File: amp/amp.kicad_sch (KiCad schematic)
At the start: 0 parts

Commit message: Initial circuit design (#2)
- Adds project description in README.md
- Populates schematic with initial circuit design
- Includes headphone output
- Adds future design to-dos
- Credits other designs influencing this project
- Extends ERC pre-commit triggers to any kicad file.
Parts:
- added C1, C5: 10nF, symbol Device:C
- added C2, C4: 2.2uF, symbol Device:C_Polarized
- added C3: 1nF, symbol Device:C
- added C6, C9: 100nF, symbol Device:C
- added C7: 220uF, symbol Device:C_Polarized
- added C8: 47nF, symbol Device:C
- added J1: Input, symbol Connector_Audio:AudioJack2
- added J2: Speaker 8Ω, symbol Connector_Audio:AudioJack2
- added J3: Headphones, symbol Connector_Audio:AudioJack2_SwitchT
- added R1, R2, R3, R4, R6, R9: 1M, symbol Device:R
- added R10, R7: 100, symbol Device:R
- added R11, R8: 220K, symbol Device:R
- added R12, R15: 10, symbol Device:R
- added R13, R14: 10K, symbol Device:R
- added R5: 47K, symbol Device:R
- added RV1: 500k log, symbol Device:R_Potentiometer
- added RV2: 50k log, symbol Device:R_Potentiometer
- added U1: NE5532, symbol Amplifier_Operational:NE5532
- added U3: LM386, symbol Amplifier_Audio:LM386
- added V1: 12AX7, Valve:Valve_Noval_P, symbol Valve:ECC83
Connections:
- new net: C1.2, R1.2, U1.3 (+)
- new net: C2.1, R2.1
- new net: R7.2, V1.8 (K)
- new net: R2.2, RV1.1, U1.2 (-)
- new net: J2.T, J3.TN
- new net: C6.1, R11.1, V1.1 (A)
- new net: C6.2, RV2.1
- new net: R10.2, V1.3 (K)
- new net: R13.1, R14.2, U1.5 (+)
- new net: RV2.2, U3.2 (-)
- new net: C7.1, R12.2, U3.5
- new net: C9.2, U3.7 (BYPASS)
- new net: C5.1, R8.1, V1.6 (A)
- new net: C7.2, J3.T
- new net: C1.1, J1.T
- new net: C3.2, R5.2, R6.2
- new net: U1.6 (-), U1.7
- new net: J3.S, R15.2
- new net: C3.1, RV1.2, U1.1
- new net: R5.1, V1.7 (G)
- new net: C5.2, R9.2, V1.2 (G)
- new net: C8.2, R12.1
- new net +12V: R11.2, R13.2, R4.2, R8.2, U1.8 (V+), U3.6 (V+), V1.4 (F1)
- new net +6V bias: C4.1, R1.1, R3.2, R4.1
- new net GND: C2.2, C4.2, C8.1, C9.1, J1.S, J2.S, R10.1, R14.1, R15.1, R3.1, R6.1, R7.1, R9.1, RV2.3, U1.4 (V-), U3.3 (+), U3.4 (GND), V1.5 (F1)
- no-connect marks 0 -> 4
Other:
- note added: "Zobel"

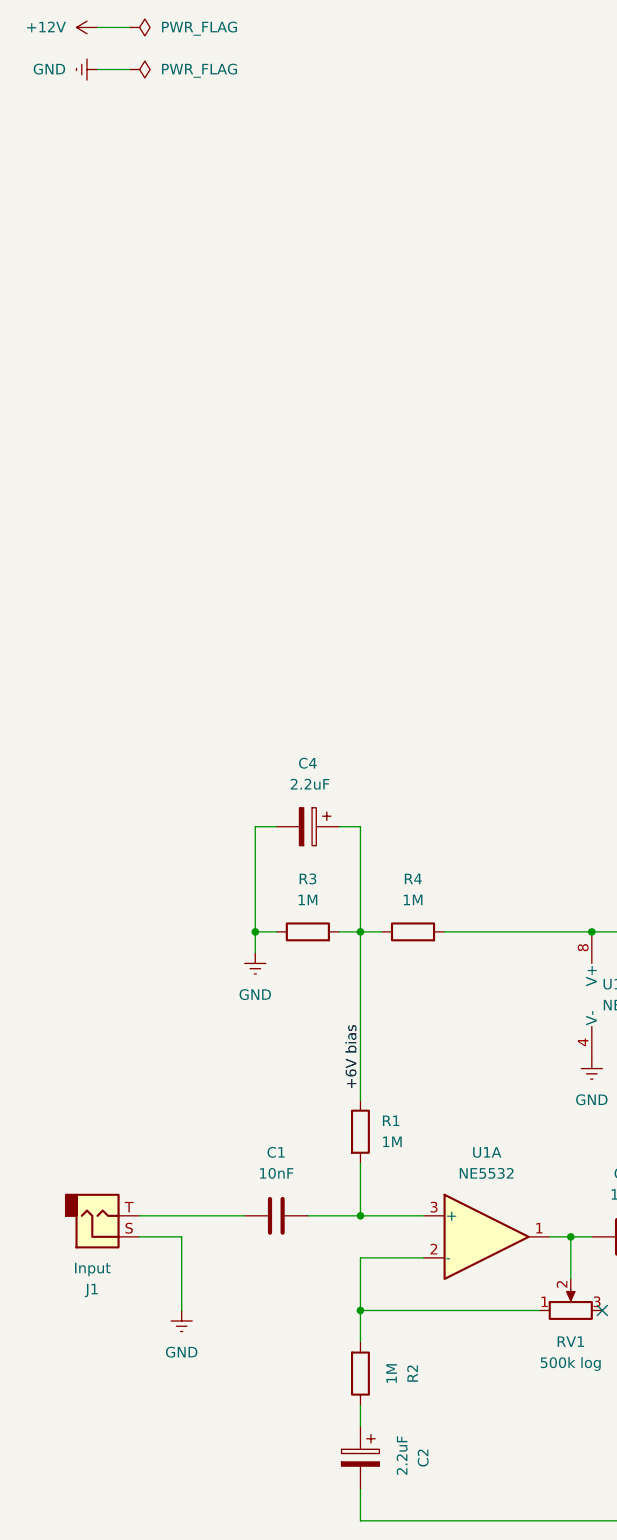
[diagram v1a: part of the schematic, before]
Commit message: Add 6V bias net, simplify cap choice, fix input buffer gain resistor
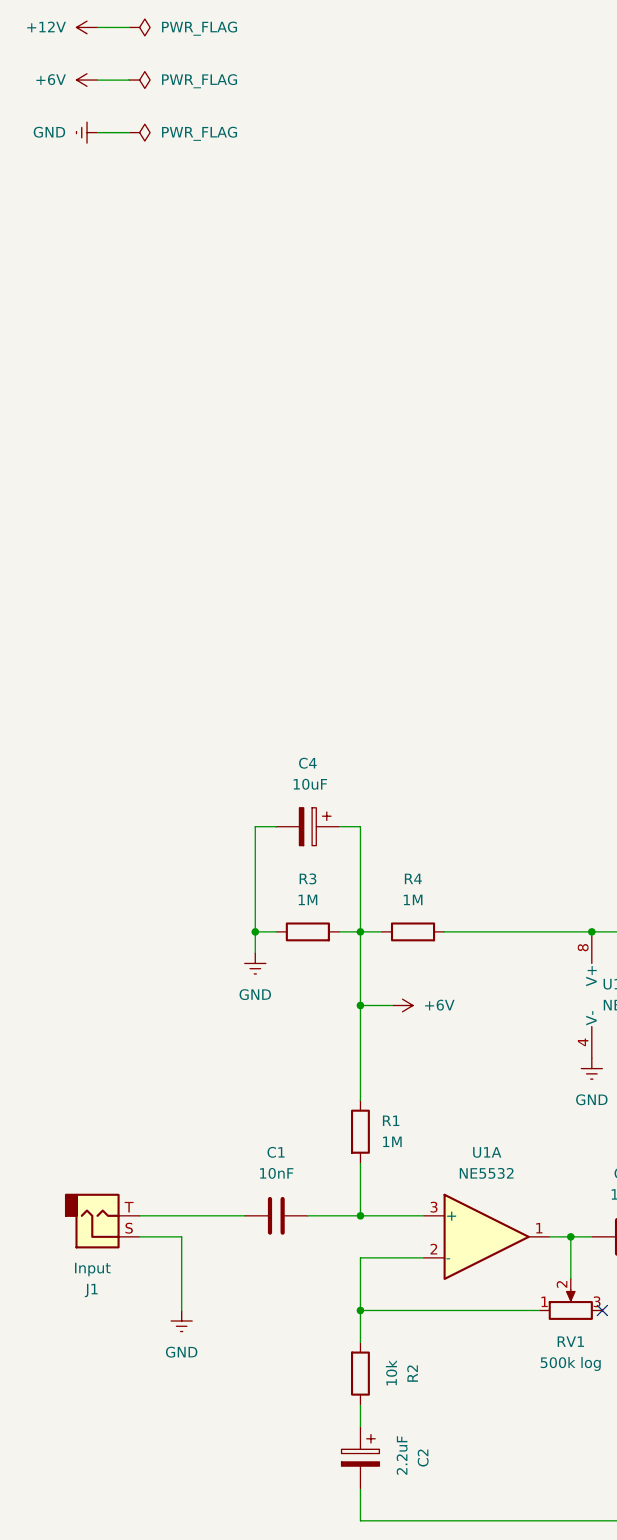
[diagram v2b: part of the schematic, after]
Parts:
- C4: value 2.2uF -> 10uF
- R2: value 1M -> 10k
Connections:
- net +6V bias renamed +6V

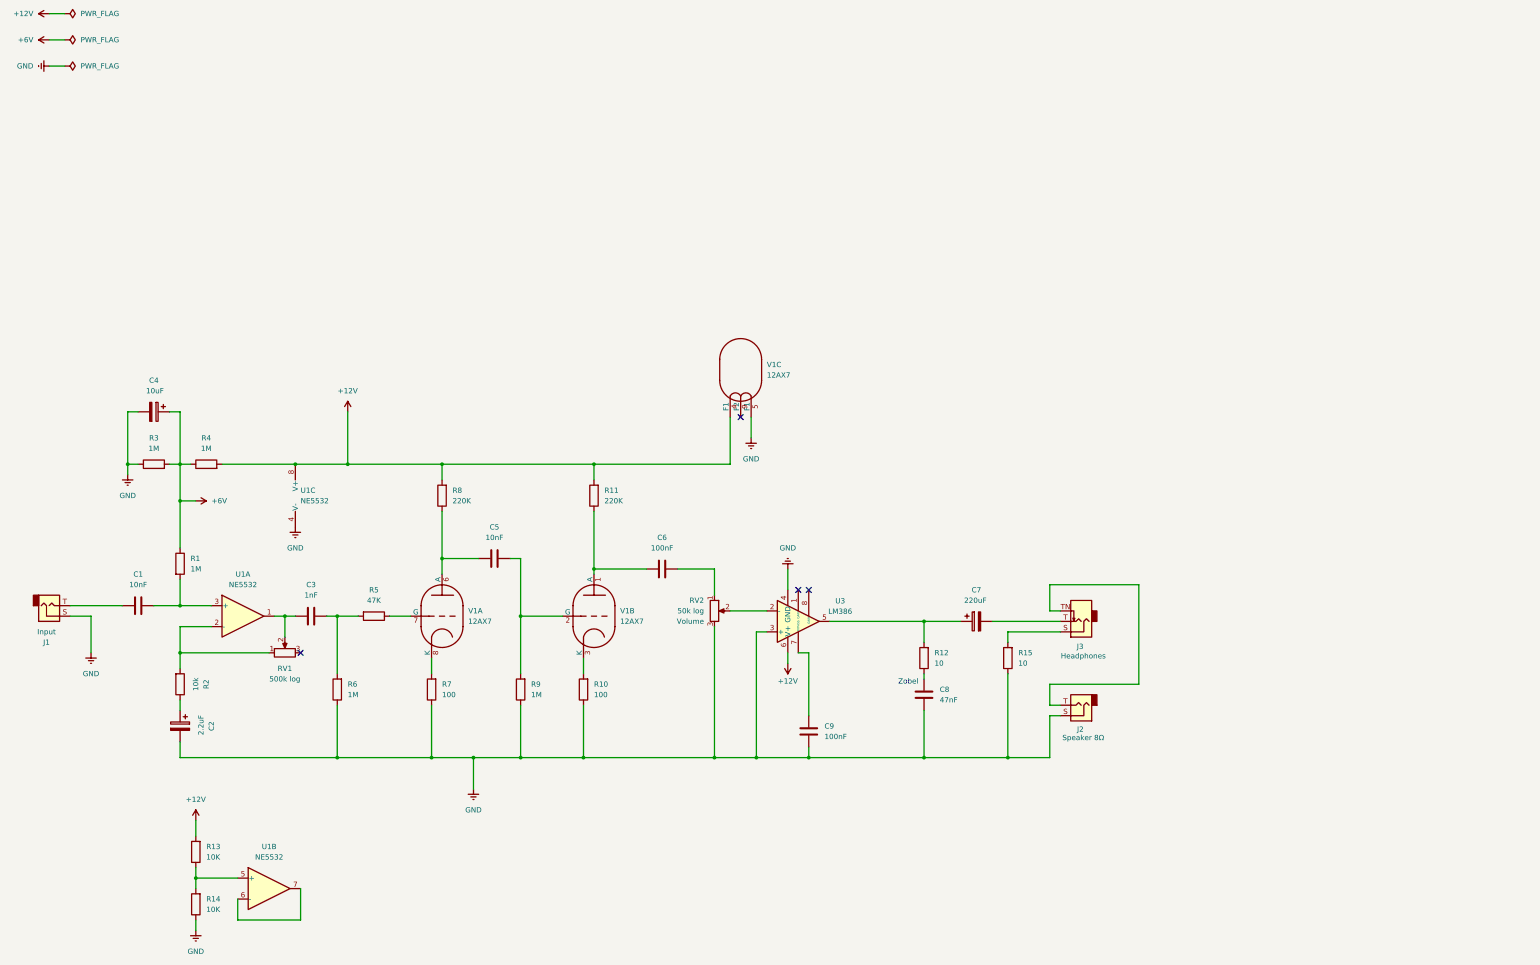
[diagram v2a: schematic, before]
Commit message: Always on FX loop
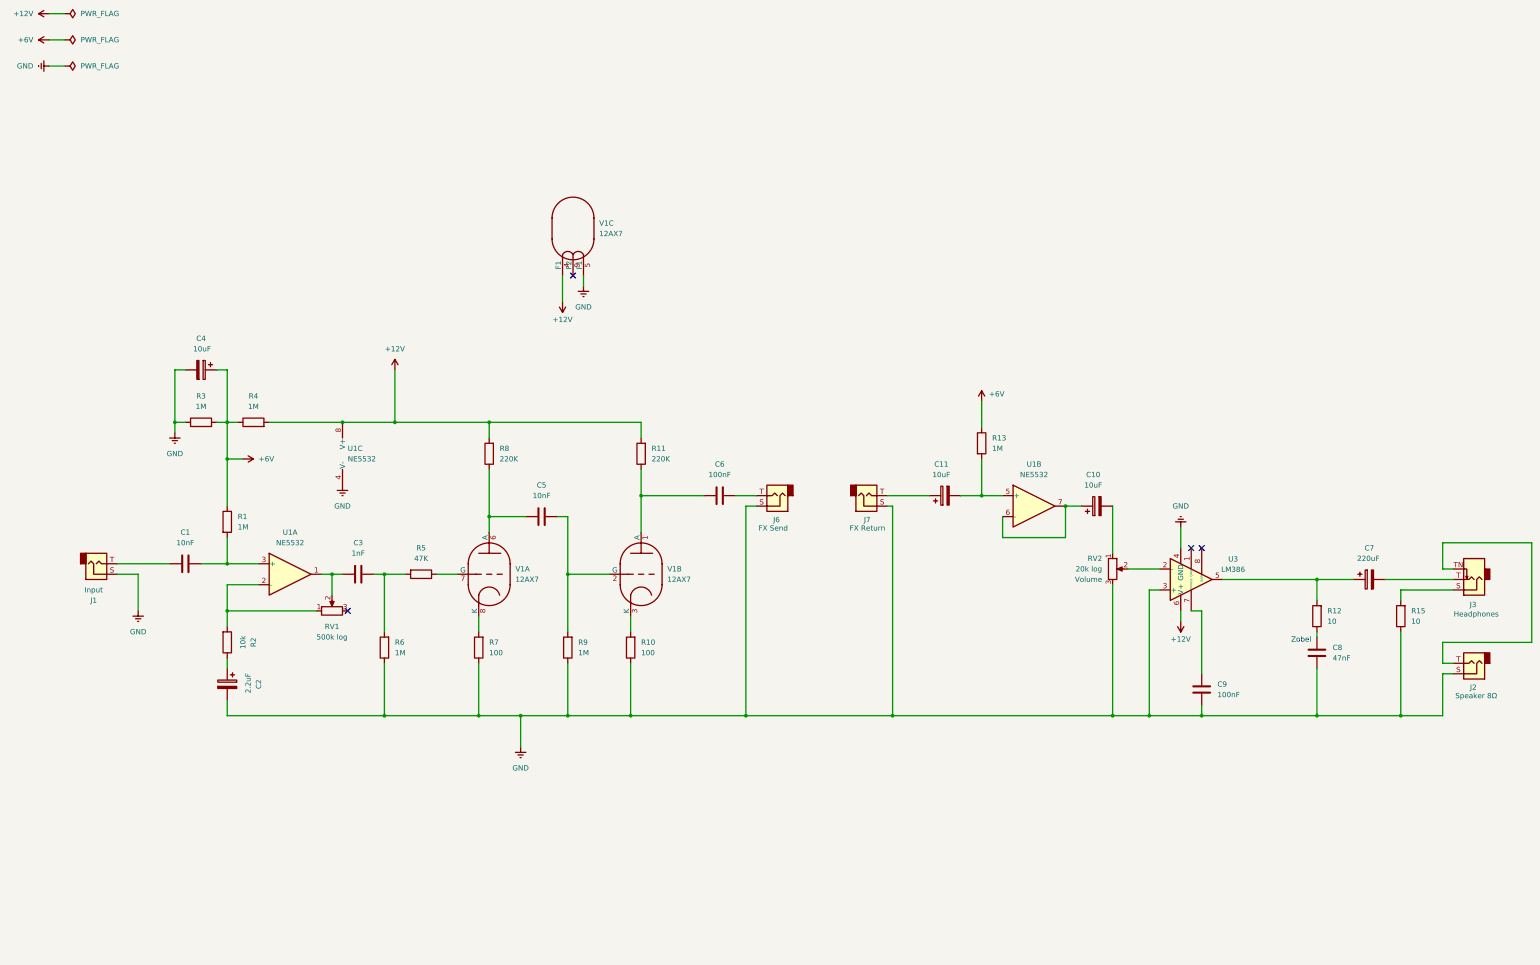
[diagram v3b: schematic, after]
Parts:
- removed R14: 10K, symbol Device:R
- added C10, C11: 10uF, symbol Device:C_Polarized
- added J6: FX Send, symbol Connector_Audio:AudioJack2
- added J7: FX Return, symbol Connector_Audio:AudioJack2
- R13: value 10K -> 1M
- RV2: value 50k log -> 20k log
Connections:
- net +12V: no longer R13.2
- net +6V: now also R13.1
- net GND: now also J6.S, J7.S
- net at RV2.1: now also C10.2; no longer C6.2
- net at U1.5 (+): now also R13.2, C11.2; no longer R13.1
- net at U1.6 (-), U1.7: now also C10.1
- new net: C6.2, J6.T
- new net: C11.1, J7.T
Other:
- moved on the sheet: C1, C2, C3, C4, C5, C6, C7, C8, C9, J1, J2, J3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

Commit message: FX Enable/Bypass switch
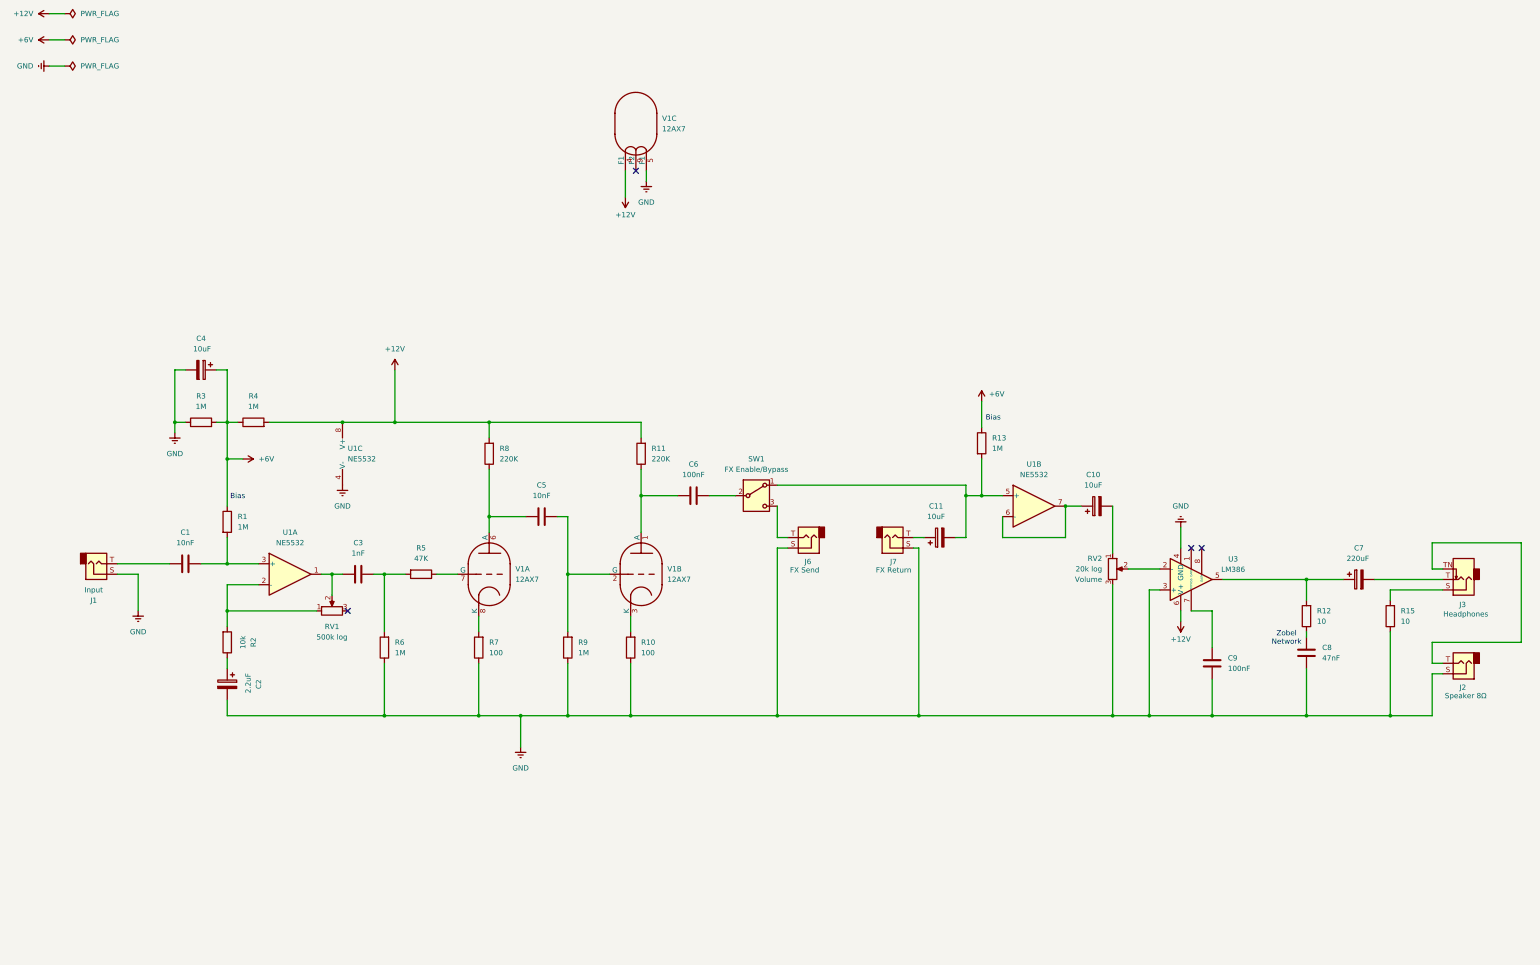
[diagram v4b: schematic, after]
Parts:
- added SW1: FX Enable/Bypass, symbol Switch:SW_SPDT
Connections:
- net at J6.T: now also SW1.3 (C); no longer C6.2
- net at C11.2, R13.2, U1.5 (+): now also SW1.1 (A)
- new net: C6.2, SW1.2 (B)
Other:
- note added: "Bias"
- note added: "Zobel Network"
- note removed: "Zobel"
- moved on the sheet: C11, C6, C7, C8, C9, J2, J3, J6, J7, R12, R15, V1C

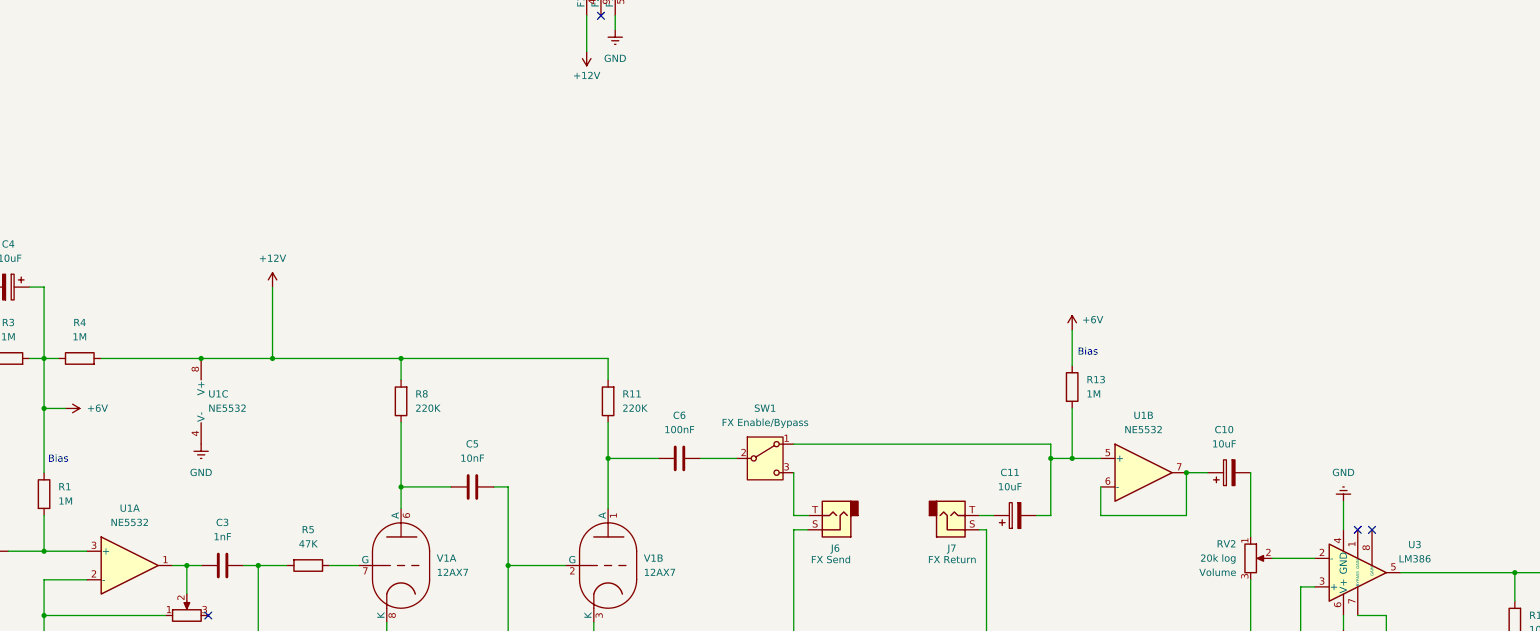
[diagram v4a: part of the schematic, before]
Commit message: Add bypass caps (#11)
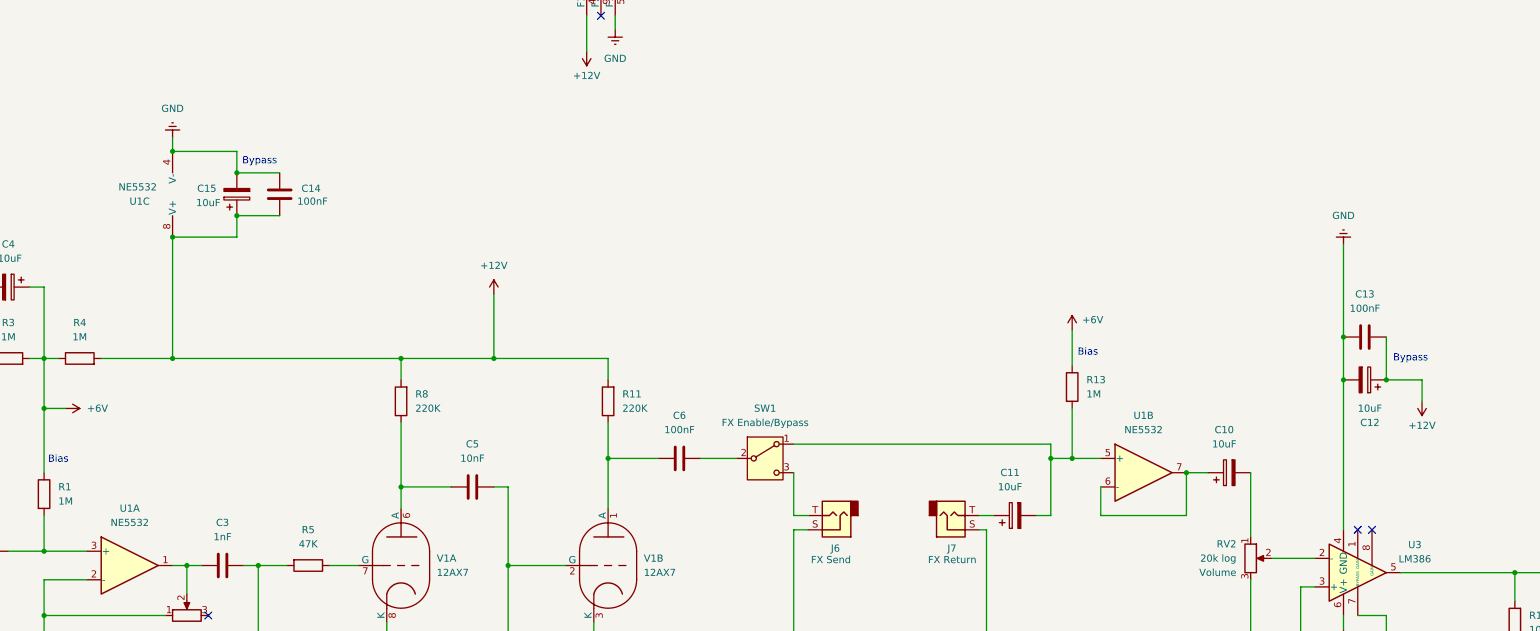
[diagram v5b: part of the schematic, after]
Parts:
- added C12, C15: 10uF, symbol Device:C_Polarized
- added C13, C14: 100nF, symbol Device:C
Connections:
- net +12V: now also C12.1, C13.2, C14.2, C15.1
- net GND: now also C12.2, C13.1, C14.1, C15.2
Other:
- note added: "Bypass"
- moved on the sheet: U1C
